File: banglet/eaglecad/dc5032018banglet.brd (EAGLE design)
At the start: 39.8 x 22.6 mm, 39 parts, among them Q3 DMG3415U-7, U2 AP2112(3.3V), U3 MCP73831T-2ACI/OT, U4 CP2104, X1 32.768, X2 JSTPH, X4 20329

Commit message: Removed cap and replaced JST connector with vias
VPP on the UART is for a one time ROM programming of the UART
which we don't need, so removing it.

We were unable to find batteries that came with the JST female
connectors that went with the used board mounted connector.
Replacing it with vias to use with either board mounted breakaway
header or something else which will fit.

Signed-off-by: nisha <nishakumarx@gmail.com>
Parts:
- removed C7: 10uf, microbuilder:0805-NO
- removed X2: JSTPH, microbuilder:JSTPH2
- added JST: (no value), SparkFun-Connectors:1X02
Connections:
- removed net N$14: C7.1, U4.16
- net GND: now also JST.1; no longer C7.2, X2.1
- net VBAT: now also JST.2; no longer X2.2
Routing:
- net N$14: track 4.87 -> 0.00 mm
- net GND: track 52.6 -> 54.2 mm, vias 29 -> 28
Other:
- board text added: "#banglet 2018 @nishakmr Thanks to: Adafruit Industries OSHPark"
- board text added: "VBAT"
- board text removed: "DC503 Banglet DefCon26 nishak"
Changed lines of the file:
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@@
 <text x="17.272" y="50.546" size="0.4064" layer="21">CHIPLED_0805</text>
 <text x="10.922" y="33.274" size="0.4064" layer="21">XTAL3215</text>
-<text x="30.226" y="36.576" size="0.6096" layer="22" rot="MR0">DC503 Banglet
-DefCon26
-nishak</text>
+<text x="33.274" y="32.131" size="0.6096" layer="22" rot="MR0">#banglet 2018
+@nishakmr
+Thanks to:
+Adafruit Industries
+OSHPark</text>
+<text x="29.21" y="32.639" size="0.8128" layer="21" rot="R90">GND</text>
+<text x="31.75" y="32.385" size="0.8128" layer="21" rot="R90">VBAT</text>
 </plain>
 <attributes>
@@
 <attribute name="VALUE" x="20.574" y="43.688" size="0.4064" layer="27" ratio="10" rot="R270"/>
 </element>
-<element name="C7" library="microbuilder" package="0805-NO" value="10uf" x="34.798" y="43.942" smashed="yes" rot="R90">
-<attribute name="NAME" x="33.909" y="42.164" size="0.8128" layer="25" ratio="18" rot="R90"/>
-<attribute name="VALUE" x="35.306" y="45.72" size="0.4064" layer="27" ratio="10" rot="R90"/>
-</element>
 <element name="C8" library="microbuilder" package="0805-NO" value="10µF" x="18.796" y="39.37" smashed="yes" rot="R180">
 <attribute name="NAME" x="16.256" y="40.005" size="0.8128" layer="25" ratio="18" rot="R270"/>
@@
 <attribute name="VALUE" x="15.046" y="34.868" size="1.016" layer="27" font="vector" rot="R180"/>
 </element>
-<element name="X2" library="microbuilder" package="JSTPH2" value="JSTPH" x="29.972" y="34.798" rot="R180"/>
 <element name="X4" library="microbuilder" package="MICRO-USB5+6P-SMD-0.65-B" value="20329" x="31.75" y="48.768" smashed="yes" rot="R180">
 <attribute name="NAME" x="32.639" y="53.594" size="0.889" layer="25" ratio="11" rot="R180"/>
@@
 <element name="FD1" library="SparkFun-Aesthetics" library_urn="urn:adsk.eagle:library:507" package="FIDUCIAL-MICRO" package3d_urn="urn:adsk.eagle:package:37111/1" value="FIDUCIALUFIDUCIAL" x="5.334" y="32.004"/>
 <element name="FD2" library="SparkFun-Aesthetics" library_urn="urn:adsk.eagle:library:507" package="FIDUCIAL-MICRO" package3d_urn="urn:adsk.eagle:package:37111/1" value="FIDUCIALUFIDUCIAL" x="39.116" y="53.086"/>
+<element name="JST" library="SparkFun-Connectors" library_urn="urn:adsk.eagle:library:513" package="1X02" package3d_urn="urn:adsk.eagle:package:38039/1" value="" x="28.829" y="36.83"/>
 </elements>
 <signals>
@@
 <contactref element="U2" pad="2"/>
 <contactref element="R12" pad="1"/>
-<contactref element="X2" pad="1"/>
 <contactref element="C5" pad="2"/>
 <contactref element="R8" pad="2"/>
@@
 <contactref element="U4" pad="2"/>
 <contactref element="C10" pad="2"/>
-<contactref element="C7" pad="2"/>
 <contactref element="SWD" pad="1"/>
 <contactref element="U1" pad="P16"/>
@@
 <via x="9.652" y="39.116" extent="1-16" drill="0.35"/>
 <via x="23.622" y="38.1" extent="1-16" drill="0.35"/>
-<via x="30.988" y="35.052" extent="1-16" drill="0.35"/>
 <via x="25.146" y="33.528" extent="1-16" drill="0.35"/>
 <via x="34.798" y="46.228" extent="1-16" drill="0.35"/>
@@
 <wire x1="5.17" y1="38.698" x2="5.588" y2="39.116" width="0.1524" layer="1"/>
 <via x="16.764" y="50.546" extent="1-16" drill="0.35"/>
-<wire x1="30.972" y1="38.498" x2="30.972" y2="35.068" width="0.254" layer="1"/>
-<wire x1="30.972" y1="35.068" x2="30.988" y2="35.052" width="0.254" layer="1"/>
 <wire x1="24.384" y1="50.8" x2="23.622" y2="50.038" width="0.254" layer="16"/>
 <wire x1="23.622" y1="50.038" x2="23.622" y2="49.276" width="0.254" layer="16"/>
@@
 <wire x1="31.5468" y1="46.482" x2="31.484" y2="46.45" width="0.1524" layer="1"/>
 <wire x1="34.7472" y1="46.2534" x2="34.798" y2="46.228" width="0.1524" layer="1"/>
+<contactref element="JST" pad="1"/>
+<wire x1="25.146" y1="33.528" x2="28.448" y2="36.83" width="0.254" layer="1"/>
+<wire x1="28.448" y1="36.83" x2="28.829" y2="36.83" width="0.1524" layer="1"/>
 </signal>
 <signal name="3.3V" class="1">
@@
 <signal name="VBAT" class="1">
 <contactref element="Q3" pad="3"/>
-<contactref element="X2" pad="2"/>
 <contactref element="U3" pad="3"/>
 <contactref element="C5" pad="1"/>
 <contactref element="R4" pad="1"/>
 <contactref element="JP3" pad="3"/>
-<wire x1="28.972" y1="38.498" x2="28.972" y2="34.814" width="0.254" layer="1"/>
-<wire x1="28.972" y1="34.814" x2="28.956" y2="34.798" width="0.254" layer="1"/>
-<via x="28.956" y="34.798" extent="1-16" drill="0.35"/>
-<wire x1="28.956" y1="34.798" x2="29.8196" y2="34.798" width="0.254" layer="16"/>
-<wire x1="33.8836" y1="38.862" x2="29.8196" y2="34.798" width="0.254" layer="16"/>
+<via x="27.051" y="38.1" extent="1-16" drill="0.35"/>
+<wire x1="27.051" y1="38.1" x2="27.9146" y2="38.862" width="0.254" layer="16"/>
+<wire x1="33.8836" y1="38.862" x2="27.9146" y2="38.862" width="0.254" layer="16"/>
 <wire x1="26.924" y1="41.468" x2="27.752" y2="40.64" width="0.254" layer="1"/>
 <wire x1="27.752" y1="40.64" x2="28.956" y2="40.64" width="0.254" layer="1"/>
-<wire x1="28.956" y1="40.64" x2="28.972" y2="40.624" width="0.254" layer="1"/>
-<wire x1="28.972" y1="40.624" x2="28.972" y2="38.498" width="0.254" layer="1"/>
 <wire x1="23.622" y1="41.164" x2="23.352" y2="40.894" width="0.254" layer="1"/>
 <wire x1="23.352" y1="40.894" x2="22.352" y2="40.894" width="0.254" layer="1"/>
@@
 <via x="26.924" y="40.132" extent="1-16" drill="0.35"/>
 <wire x1="26.924" y1="40.132" x2="26.924" y2="41.468" width="0.254" layer="1"/>
-<wire x1="24.572" y1="36.7999" x2="24.572" y2="35.56" width="0.254" layer="1"/>
-<wire x1="24.572" y1="35.56" x2="24.572" y2="34.898" width="0.254" layer="1"/>
+<wire x1="24.572" y1="36.7999" x2="24.572" y2="35.687" width="0.254" layer="1"/>
+<wire x1="24.572" y1="35.687" x2="24.572" y2="34.898" width="0.254" layer="1"/>
 <wire x1="24.572" y1="34.898" x2="24.218" y2="34.544" width="0.254" layer="1"/>
 <wire x1="24.6888" y1="34.8996" x2="24.218" y2="34.544" width="0.254" layer="1"/>
-<wire x1="28.8798" y1="34.8996" x2="28.956" y2="34.798" width="0.254" layer="1"/>
 <wire x1="34.29" y1="38.862" x2="33.8836" y2="38.862" width="0.1524" layer="16"/>
-<wire x1="28.956" y1="34.798" x2="28.194" y2="35.56" width="0.254" layer="1"/>
-<wire x1="28.194" y1="35.56" x2="24.572" y2="35.56" width="0.254" layer="1"/>
+<wire x1="27.051" y1="38.1" x2="26.162" y2="36.576" width="0.254" layer="1"/>
+<wire x1="26.162" y1="36.576" x2="24.572" y2="35.687" width="0.254" layer="1"/>
+<contactref element="JST" pad="2"/>
+<wire x1="28.956" y1="40.64" x2="31.369" y2="38.227" width="0.254" layer="1"/>
+<wire x1="31.369" y1="38.227" x2="31.369" y2="37.973" width="0.1524" layer="1"/>
+<wire x1="31.369" y1="37.973" x2="31.369" y2="36.83" width="0.254" layer="1"/>
+<wire x1="26.924" y1="40.132" x2="27.051" y2="40.005" width="0.1524" layer="1"/>
+<wire x1="27.051" y1="40.005" x2="27.051" y2="38.1" width="0.254" layer="1"/>
 </signal>
 <signal name="EN">
@@
 <via x="21.5646" y="50.292" extent="1-16" drill="0.254"/>
 </signal>
-<signal name="N$14" class="1">
-<contactref element="U4" pad="16"/>
-<contactref element="C7" pad="1"/>
-<wire x1="31.0134" y1="41.9862" x2="31.0134" y2="42.4434" width="0.254" layer="1"/>
-<wire x1="31.242" y1="41.7576" x2="31.0134" y2="41.9862" width="0.254" layer="1"/>
-<wire x1="33.528" y1="41.7576" x2="31.242" y2="41.7576" width="0.254" layer="1"/>
-<wire x1="34.7472" y1="42.9768" x2="33.528" y2="41.7576" width="0.254" layer="1"/>
-<wire x1="31.0134" y1="42.4434" x2="30.984" y2="42.45" width="0.254" layer="1"/>
-<wire x1="34.7472" y1="42.9768" x2="34.798" y2="42.992" width="0.254" layer="1"/>
-</signal>
 <signal name="SWDIO">

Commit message: Simplify vbat due to through hole.
tent vias
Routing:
- net VBAT: track 31.0 -> 27.2 mm, vias 3 -> 2
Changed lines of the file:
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@@
 </class>
 </classes>
-<designrules name="oshpark-2layer">
+<designrules name="oshpark-2layer *">
 <description language="en">&lt;b&gt;OSH Park Design Rules&lt;/b&gt;
 &lt;p&gt;
@@
 <param name="mlMinCreamFrame" value="0mil"/>
 <param name="mlMaxCreamFrame" value="0mil"/>
-<param name="mlViaStopLimit" value="0mil"/>
+<param name="mlViaStopLimit" value="25mil"/>
 <param name="srRoundness" value="0"/>
 <param name="srMinRoundness" value="0mil"/>
@@
 <contactref element="R4" pad="1"/>
 <contactref element="JP3" pad="3"/>
-<via x="27.051" y="38.1" extent="1-16" drill="0.35"/>
-<wire x1="27.051" y1="38.1" x2="27.9146" y2="38.862" width="0.254" layer="16"/>
-<wire x1="33.8836" y1="38.862" x2="27.9146" y2="38.862" width="0.254" layer="16"/>
 <wire x1="26.924" y1="41.468" x2="27.752" y2="40.64" width="0.254" layer="1"/>
 <wire x1="27.752" y1="40.64" x2="28.956" y2="40.64" width="0.254" layer="1"/>
@@
 <wire x1="24.572" y1="34.898" x2="24.218" y2="34.544" width="0.254" layer="1"/>
 <wire x1="24.6888" y1="34.8996" x2="24.218" y2="34.544" width="0.254" layer="1"/>
-<wire x1="34.29" y1="38.862" x2="33.8836" y2="38.862" width="0.1524" layer="16"/>
+<wire x1="33.8836" y1="38.862" x2="34.29" y2="38.862" width="0.1524" layer="16"/>
 <wire x1="27.051" y1="38.1" x2="26.162" y2="36.576" width="0.254" layer="1"/>
 <wire x1="26.162" y1="36.576" x2="24.572" y2="35.687" width="0.254" layer="1"/>
 <contactref element="JST" pad="2"/>
-<wire x1="28.956" y1="40.64" x2="31.369" y2="38.227" width="0.254" layer="1"/>
-<wire x1="31.369" y1="38.227" x2="31.369" y2="37.973" width="0.1524" layer="1"/>
-<wire x1="31.369" y1="37.973" x2="31.369" y2="36.83" width="0.254" layer="1"/>
-<wire x1="26.924" y1="40.132" x2="27.051" y2="40.005" width="0.1524" layer="1"/>
-<wire x1="27.051" y1="40.005" x2="27.051" y2="38.1" width="0.254" layer="1"/>
+<wire x1="31.369" y1="38.227" x2="28.956" y2="40.64" width="0.254" layer="1"/>
+<wire x1="27.051" y1="39.878" x2="27.051" y2="38.1" width="0.254" layer="1"/>
+<wire x1="31.369" y1="36.83" x2="31.369" y2="38.227" width="0.254" layer="1"/>
+<wire x1="31.369" y1="36.83" x2="33.401" y2="38.862" width="0.254" layer="16"/>
+<wire x1="33.401" y1="38.862" x2="33.8836" y2="38.862" width="0.254" layer="16"/>
+<wire x1="26.924" y1="40.132" x2="27.051" y2="40.005" width="0.254" layer="1"/>
+<wire x1="27.051" y1="40.005" x2="27.051" y2="39.878" width="0.254" layer="1"/>
 </signal>
 <signal name="EN">

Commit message: Add banlet lib with 2.5mm part and use as J1
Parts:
- removed JST: (no value), SparkFun-Connectors:1X02
- added J1: S2B-EH(LF)(SN), banglet:1X2(2.5)
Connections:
- net GND: now also J1.1; no longer JST.1
- net VBAT: now also J1.2; no longer JST.2
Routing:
- net VBAT: track 27.2 -> 28.7 mm
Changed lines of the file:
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@@
 <element name="FD1" library="SparkFun-Aesthetics" library_urn="urn:adsk.eagle:library:507" package="FIDUCIAL-MICRO" package3d_urn="urn:adsk.eagle:package:37111/1" value="FIDUCIALUFIDUCIAL" x="5.334" y="32.004"/>
 <element name="FD2" library="SparkFun-Aesthetics" library_urn="urn:adsk.eagle:library:507" package="FIDUCIAL-MICRO" package3d_urn="urn:adsk.eagle:package:37111/1" value="FIDUCIALUFIDUCIAL" x="39.116" y="53.086"/>
-<element name="JST" library="SparkFun-Connectors" library_urn="urn:adsk.eagle:library:513" package="1X02" package3d_urn="urn:adsk.eagle:package:38039/1" value="" x="28.829" y="36.83"/>
+<element name="J1" library="banglet" package="1X2(2.5)" value="S2B-EH(LF)(SN)" x="28.829" y="36.83" smashed="yes">
+<attribute name="NAME" x="27.559" y="38.227" size="0.6096" layer="25" font="vector" ratio="20"/>
+</element>
 </elements>
 <signals>
@@
 <wire x1="31.5468" y1="46.482" x2="31.484" y2="46.45" width="0.1524" layer="1"/>
 <wire x1="34.7472" y1="46.2534" x2="34.798" y2="46.228" width="0.1524" layer="1"/>
-<contactref element="JST" pad="1"/>
 <wire x1="25.146" y1="33.528" x2="28.448" y2="36.83" width="0.254" layer="1"/>
-<wire x1="28.448" y1="36.83" x2="28.829" y2="36.83" width="0.1524" layer="1"/>
+<contactref element="J1" pad="1"/>
 </signal>
 <signal name="3.3V" class="1">
@@
 <wire x1="27.051" y1="38.1" x2="26.162" y2="36.576" width="0.254" layer="1"/>
 <wire x1="26.162" y1="36.576" x2="24.572" y2="35.687" width="0.254" layer="1"/>
-<contactref element="JST" pad="2"/>
-<wire x1="31.369" y1="38.227" x2="28.956" y2="40.64" width="0.254" layer="1"/>
-<wire x1="27.051" y1="39.878" x2="27.051" y2="38.1" width="0.254" layer="1"/>
-<wire x1="31.369" y1="36.83" x2="31.369" y2="38.227" width="0.254" layer="1"/>
-<wire x1="31.369" y1="36.83" x2="33.401" y2="38.862" width="0.254" layer="16"/>
+<wire x1="28.956" y1="40.64" x2="31.369" y2="38.227" width="0.254" layer="1"/>
+<wire x1="27.051" y1="40.005" x2="27.051" y2="38.1" width="0.254" layer="1"/>
 <wire x1="33.401" y1="38.862" x2="33.8836" y2="38.862" width="0.254" layer="16"/>
 <wire x1="26.924" y1="40.132" x2="27.051" y2="40.005" width="0.254" layer="1"/>
-<wire x1="27.051" y1="40.005" x2="27.051" y2="39.878" width="0.254" layer="1"/>
+<contactref element="J1" pad="2"/>
+<wire x1="31.369" y1="38.227" x2="31.369" y2="36.87" width="0.254" layer="1"/>
+<wire x1="31.369" y1="36.87" x2="31.329" y2="36.83" width="0.254" layer="1"/>
+<wire x1="34.29" y1="38.862" x2="32.385" y2="38.862" width="0.254" layer="16"/>
+<wire x1="32.385" y1="38.862" x2="31.329" y2="37.806" width="0.254" layer="16"/>
+<wire x1="31.329" y1="37.806" x2="31.329" y2="36.83" width="0.254" layer="16"/>
 </signal>
 <signal name="EN">

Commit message: Added new part for LED strip connection
- Added new part to banglet library
- Replaced vias for the LED strip with new part

Eaglecad refuses to name the vias after the nets in the schematic

Signed-off-by: nisha <nishakumarx@gmail.com>
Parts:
- removed A0, GND, VLED: WIREPAD2,54/0,9, wirepad:2,54/0,9
- added LEDCONN: WS2812B-LED-STRIPLEDCONN, banglet:1X3(2.5)
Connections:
- removed net N$3: JP3.2, VLED.1
- new net VLED: JP3.2, LEDCONN.1
- net A0: no longer A0.1
- net GND: no longer GND.1
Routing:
- net VLED: track 0.00 -> 9.14 mm
- net N$3: track 8.62 -> 0.00 mm
- net GND: track 53.8 -> 55.2 mm, vias 28 -> 29
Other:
- board text added: "A0"
- board text added: "VLED"

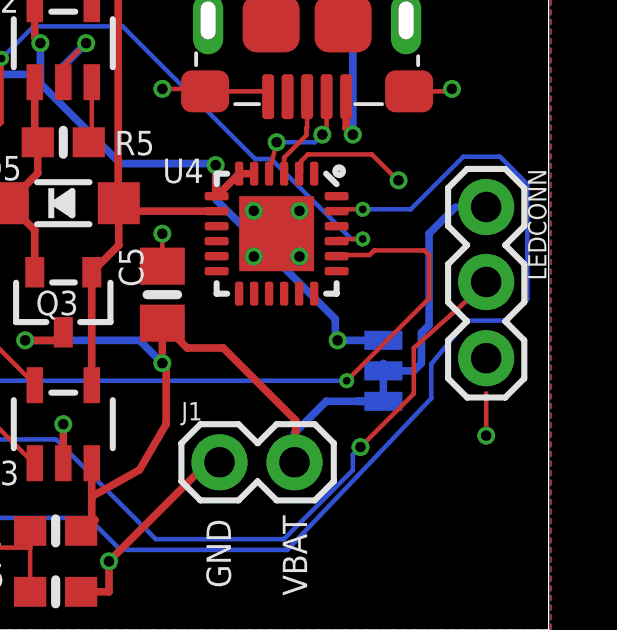
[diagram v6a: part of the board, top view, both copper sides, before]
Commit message: connect led header in schematic and board
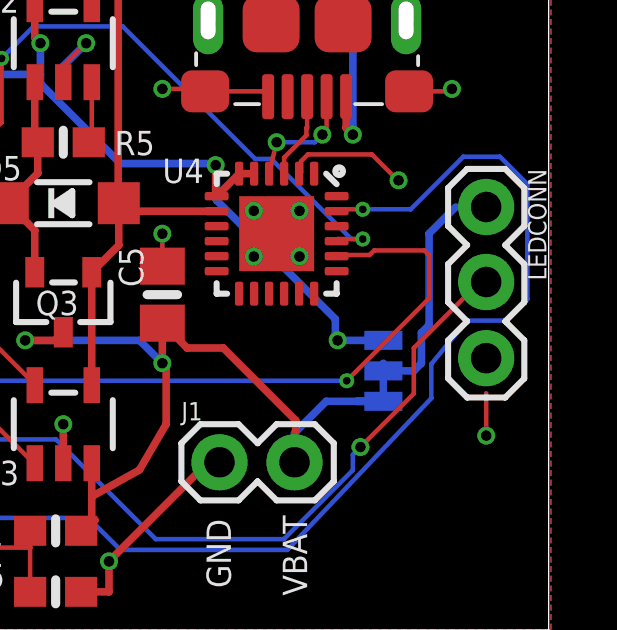
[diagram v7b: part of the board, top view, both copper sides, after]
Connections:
- net A0: now also LEDCONN.2
- net GND: now also LEDCONN.3
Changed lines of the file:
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@@
 <via x="37.719" y="37.719" extent="1-16" drill="0.35"/>
 <wire x1="37.719" y1="37.719" x2="37.719" y2="39.1306" width="0.1524" layer="1"/>
-<wire x1="32.95" y1="51.443" x2="35.05" y2="51.443" width="0" layer="19" extent="1-1"/>
-<wire x1="35.15" y1="49.195" x2="35.05" y2="51.443" width="0" layer="19" extent="1-1"/>
-<wire x1="30.55" y1="51.443" x2="32.95" y2="51.443" width="0" layer="19" extent="1-1"/>
-<wire x1="28.45" y1="51.443" x2="30.55" y2="51.443" width="0" layer="19" extent="1-1"/>
-<wire x1="28.269" y1="49.276" x2="28.45" y2="51.443" width="0" layer="19" extent="1-1"/>
-<wire x1="31.7754" y1="47.0916" x2="30.45" y2="49.018" width="0" layer="19" extent="1-1"/>
-<wire x1="31.496" y1="45.212" x2="31.484" y2="46.45" width="0" layer="19" extent="1-1"/>
-<wire x1="31.496" y1="43.688" x2="31.496" y2="45.212" width="0" layer="19" extent="1-1"/>
-<wire x1="29.972" y1="45.212" x2="31.496" y2="45.212" width="0" layer="19" extent="1-1"/>
-<wire x1="29.972" y1="43.688" x2="31.496" y2="43.688" width="0" layer="19" extent="1-1"/>
-<wire x1="24.384" y1="50.8" x2="26.924" y2="49.276" width="0" layer="19" extent="16-16"/>
-<wire x1="26.924" y1="43.368" x2="29.972" y2="43.688" width="0" layer="19" extent="1-1"/>
-<wire x1="17.946" y1="49.784" x2="23.622" y2="50.038" width="0" layer="19" extent="1-16"/>
-<wire x1="17.78" y1="49.784" x2="17.946" y2="49.784" width="0" layer="19" extent="1-16"/>
-<wire x1="13.716" y1="51.943" x2="16.764" y2="50.546" width="0" layer="19" extent="1-1"/>
-<wire x1="15.142" y1="45.622" x2="17.526" y2="49.784" width="0" layer="19" extent="1-16"/>
-<wire x1="17.846" y1="43.942" x2="15.142" y2="45.622" width="0" layer="19" extent="1-1"/>
-<wire x1="15.494" y1="40.474" x2="17.846" y2="39.69" width="0" layer="19" extent="1-1"/>
-<wire x1="17.846" y1="36.83" x2="17.846" y2="39.37" width="0" layer="19" extent="1-1"/>
-<wire x1="18.796" y1="35.56" x2="17.846" y2="36.51" width="0" layer="19" extent="1-1"/>
-<wire x1="14.478" y1="36.322" x2="17.846" y2="36.51" width="0" layer="19" extent="1-1"/>
-<wire x1="13.42" y1="36.822" x2="13.462" y2="36.83" width="0" layer="19" extent="1-16"/>
-<wire x1="12.402" y1="38.354" x2="13.42" y2="36.822" width="0" layer="19" extent="1-1"/>
-<wire x1="9.652" y1="39.116" x2="11.684" y2="39.116" width="0" layer="19" extent="1-1"/>
-<wire x1="9.652" y1="41.148" x2="9.652" y2="39.116" width="0" layer="19" extent="1-1"/>
-<wire x1="9.652" y1="43.18" x2="9.652" y2="41.148" width="0" layer="19" extent="1-1"/>
-<wire x1="7.62" y1="43.18" x2="9.652" y2="43.18" width="0" layer="19" extent="1-1"/>
-<wire x1="7.62" y1="41.148" x2="9.652" y2="41.148" width="0" layer="19" extent="1-1"/>
-<wire x1="5.588" y1="41.148" x2="7.62" y2="41.148" width="0" layer="19" extent="1-1"/>
-<wire x1="5.132" y1="39.572" x2="5.588" y2="41.148" width="0" layer="19" extent="1-1"/>
-<wire x1="7.62" y1="39.116" x2="6.27" y2="37.722" width="0" layer="19" extent="1-1"/>
-<wire x1="15.24" y1="33.186" x2="14.478" y2="36.322" width="0" layer="19" extent="1-1"/>
-<wire x1="16.256" y1="33.274" x2="15.24" y2="33.186" width="0" layer="19" extent="1-1"/>
-<wire x1="15.24" y1="32.004" x2="15.24" y2="33.186" width="0" layer="19" extent="1-1"/>
-<wire x1="13.042" y1="32.512" x2="15.24" y2="32.004" width="0" layer="19" extent="1-1"/>
-<wire x1="9.398" y1="32.258" x2="13.042" y2="32.512" width="0" layer="19" extent="1-1"/>
-<wire x1="9.398" y1="33.44" x2="9.398" y2="32.258" width="0" layer="19" extent="1-1"/>
-<wire x1="23.622" y1="36.7999" x2="18.796" y2="35.56" width="0" layer="19" extent="1-1"/>
-<wire x1="25.146" y1="33.528" x2="23.622" y2="36.7999" width="0" layer="19" extent="1-1"/>
-<wire x1="28.829" y1="36.83" x2="28.448" y2="36.83" width="0" layer="19" extent="1-1"/>
-<wire x1="37.719" y1="39.1306" x2="34.798" y2="46.228" width="0" layer="19" extent="1-1"/>
+<contactref element="LEDCONN" pad="3"/>
 </signal>
 <signal name="3.3V" class="1">
@@
 <wire x1="33.528" y1="37.338" x2="35.306" y2="39.116" width="0.1524" layer="1"/>
 <wire x1="35.306" y1="39.116" x2="35.306" y2="40.64" width="0.1524" layer="1"/>
-<wire x1="35.306" y1="40.64" x2="37.719" y2="42.799" width="0.1524" layer="1"/>
 <wire x1="33.274" y1="36.5702125" x2="33.274" y2="37.084" width="0.1524" layer="16"/>
+<contactref element="LEDCONN" pad="2"/>
+<wire x1="35.306" y1="40.64" x2="37.505" y2="42.839" width="0.1524" layer="1"/>
+<wire x1="37.505" y1="42.839" x2="37.719" y2="42.839" width="0.1524" layer="1"/>
 </signal>
 <signal name="N$1">
